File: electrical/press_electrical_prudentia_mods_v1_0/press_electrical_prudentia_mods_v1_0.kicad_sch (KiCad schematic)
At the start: 22 parts, among them J1 Mains 120V 60Hz 15Amax, J2 LCD-I2C, J3 Conn_01x06, SW1 SW_DIP_x01, SW2 RotaryEncoder_Switch, U1 34.81-9024, U1 MAX31855, U2 34.81-9024

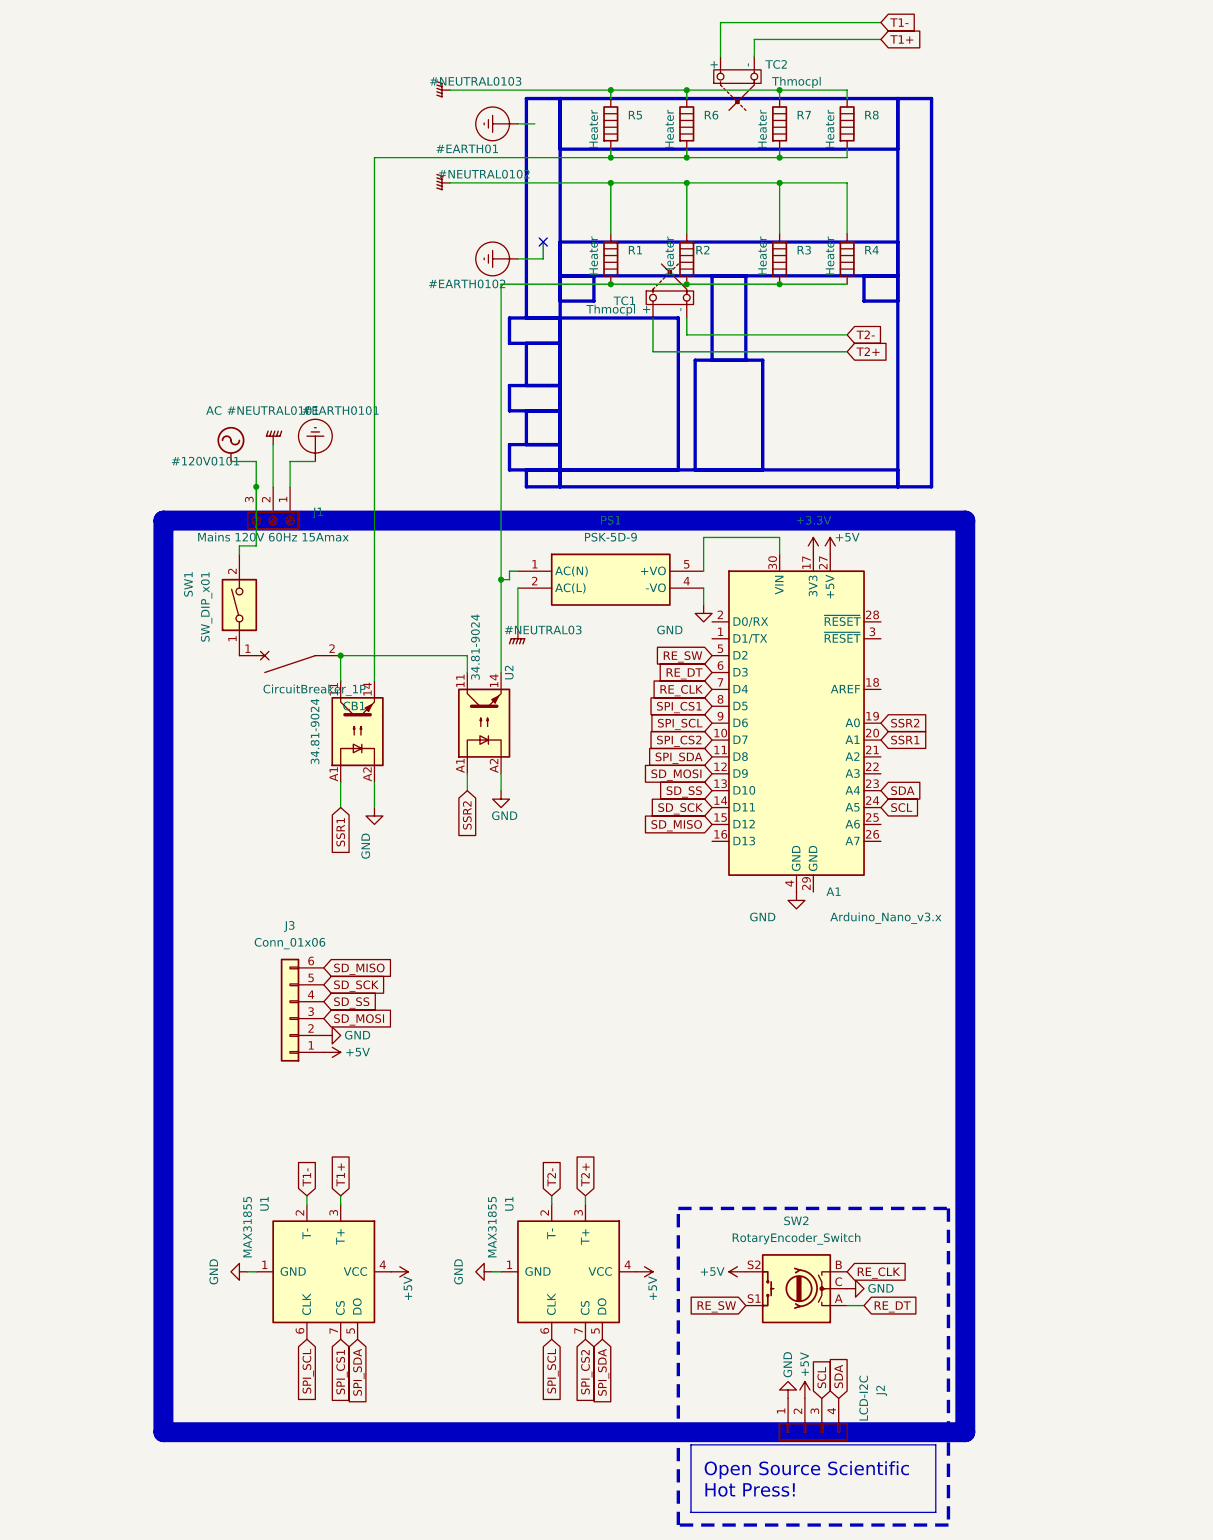
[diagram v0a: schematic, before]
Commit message: added full depth to electrical and software segmentation
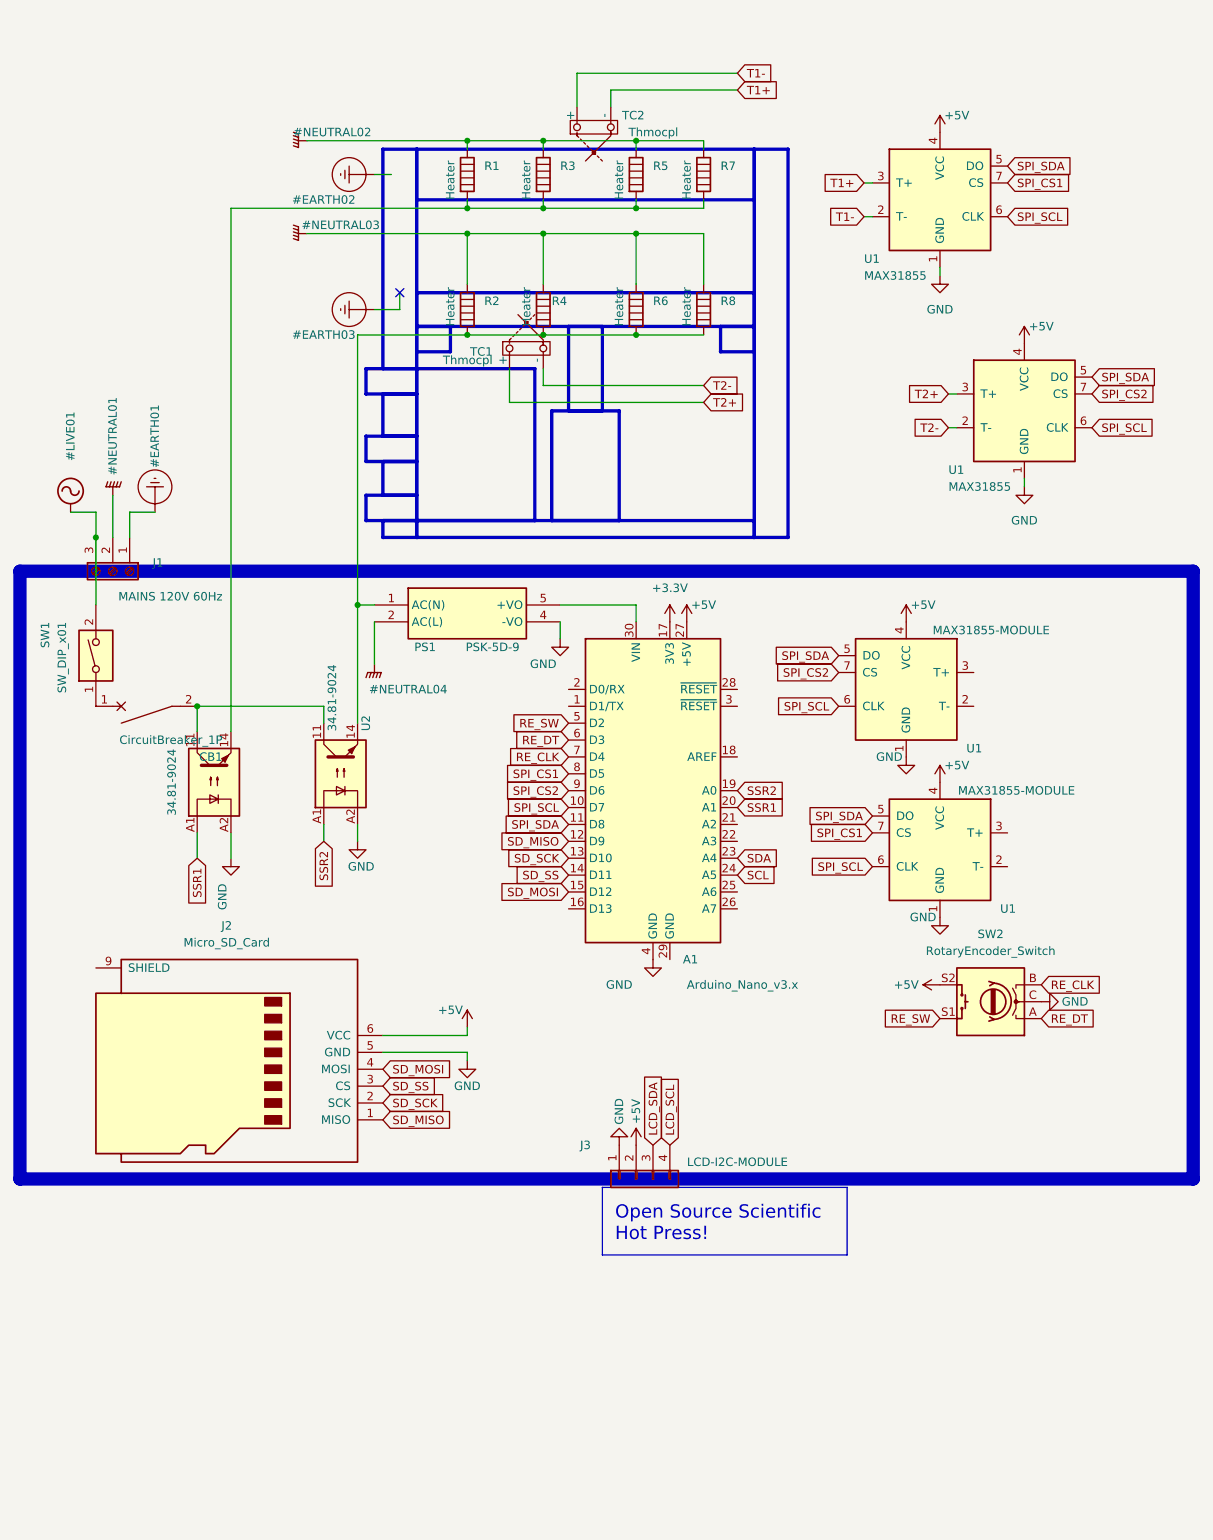
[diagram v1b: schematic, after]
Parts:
- removed J2: LCD-I2C, Connector_PinSocket_2.54mm:PinSocket_1x04_P2.54mm_Vertical, symbol Connector_Generic:Conn_01x04
- removed J3: Conn_01x06, symbol Connector_Generic:Conn_01x06
- removed U1 (x2): MAX31855, Package_SO:SOIC-8_3.9x4.9mm_P1.27mm, symbol Sensor_Temperature:MAX31855EASA
- added J2: Micro_SD_Card, symbol Connector:Micro_SD_Card
- added J3: LCD-I2C-MODULE, Connector_PinSocket_2.54mm:PinSocket_1x04_P2.54mm_Vertical, symbol Connector_Generic:Conn_01x04
- added U1 (x2): MAX31855, Package_SO:SOIC-8_3.9x4.9mm_P1.27mm, symbol Sensor_Temperature:MAX31855EASA
- added U1 (x2): MAX31855-MODULE, Package_SO:SOIC-8_3.9x4.9mm_P1.27mm, symbol Sensor_Temperature:MAX31855EASA
- J1: value Mains 120V 60Hz 15Amax -> MAINS 120V 60Hz
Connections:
- net +5V: now also J2.6 (VCC), J3.2 (Pin_2), U1.4 (VCC), U1.4 (VCC), U1.4 (VCC), U1.4 (VCC)
- net GND: now also J2.5 (GND), J3.1 (Pin_1), U1.1 (GND), U1.1 (GND), U1.1 (GND), U1.1 (GND)
- net SD_MISO: now also A1.12 (D9), J2.1 (MISO); no longer A1.15 (D12)
- net SD_MOSI: now also A1.15 (D12), J2.4 (MOSI); no longer A1.12 (D9)
- net SD_SCK: now also A1.13 (D10), J2.2 (SCK); no longer A1.14 (D11)
- net SD_SS: now also A1.14 (D11), J2.3 (CS); no longer A1.13 (D10)
- net SPI_CS1: now also U1.7 (CS), U1.7 (CS)
- net SPI_CS2: now also A1.9 (D6), U1.7 (CS), U1.7 (CS); no longer A1.10 (D7)
- net SPI_SCL: now also A1.10 (D7), U1.6 (CLK), U1.6 (CLK), U1.6 (CLK), U1.6 (CLK); no longer A1.9 (D6)
- net SPI_SDA: now also U1.5 (DO), U1.5 (DO), U1.5 (DO), U1.5 (DO)
- net T1+: now also U1.3 (T+)
- net T1-: now also U1.2 (T-)
- net T2+: now also U1.3 (T+)
- net T2-: now also U1.2 (T-)
- net at PS1.1 (AC(N)), R2.2, R4.2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: now also R6.2, R8.2; no longer R1.2, R3.2
- net at R5.2, R7.2, U1.14: now also R1.2, R3.2; no longer R6.2, R8.2
- new net LCD_SCL: J3.4 (Pin_4)
- new net LCD_SDA: J3.3 (Pin_3)
